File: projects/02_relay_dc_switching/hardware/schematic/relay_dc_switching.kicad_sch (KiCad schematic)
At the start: 9 parts, among them K1 JQC-3FF-S-Z, SW2 SW_MEC_5E

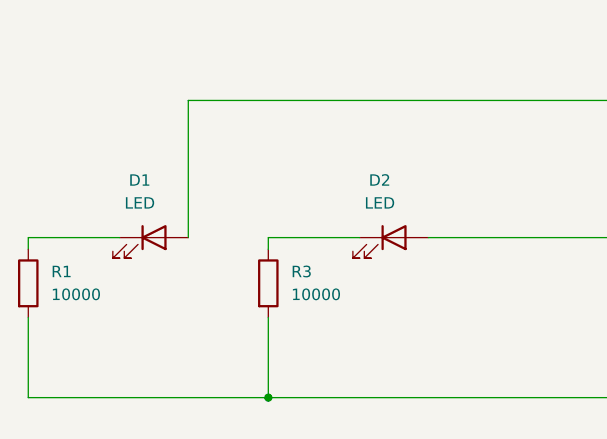
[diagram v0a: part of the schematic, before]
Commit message: refactor(hardware): update resistor values in circuit schemma in project 02
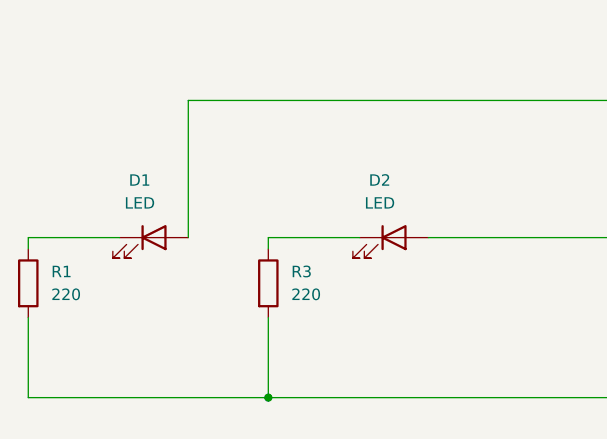
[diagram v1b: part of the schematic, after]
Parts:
- R1, R3: value 10000 -> 220

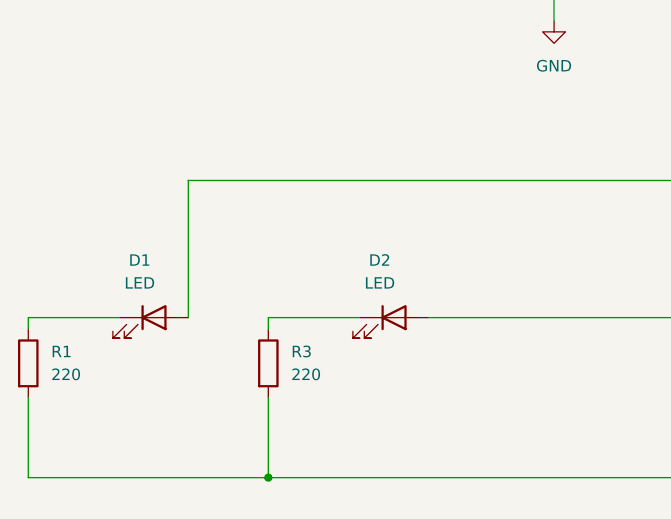
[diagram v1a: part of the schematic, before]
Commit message: refactor(hardware): update led color naming in circuit schmma on project 02
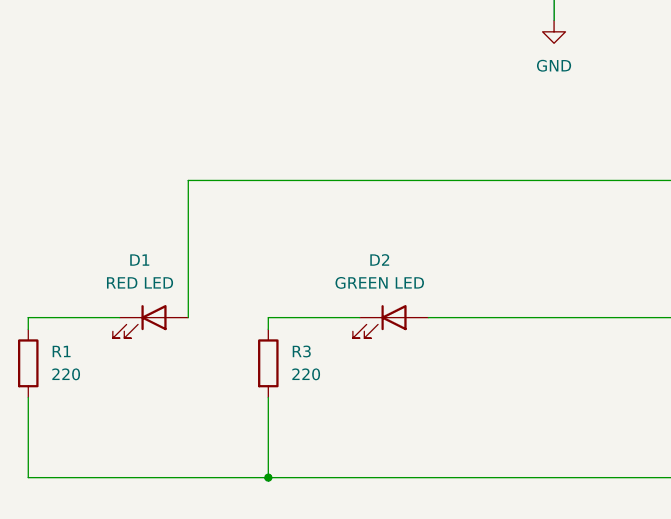
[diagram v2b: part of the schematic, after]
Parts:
- D1: value LED -> RED LED
- D2: value LED -> GREEN LED
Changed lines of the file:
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@@
 			)
 		)
-		(property "Value" "LED"
+		(property "Value" "RED LED"
 			(at 37.7825 90.17 0)
 			(effects
@@
 			)
 		)
-		(property "Value" "LED"
+		(property "Value" "GREEN LED"
 			(at 64.4525 90.17 0)
 			(effects
